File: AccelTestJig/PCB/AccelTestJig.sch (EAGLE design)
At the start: 11 parts, among them Q1 MMBTA56-SOT23, U1 MMA8653FCR1

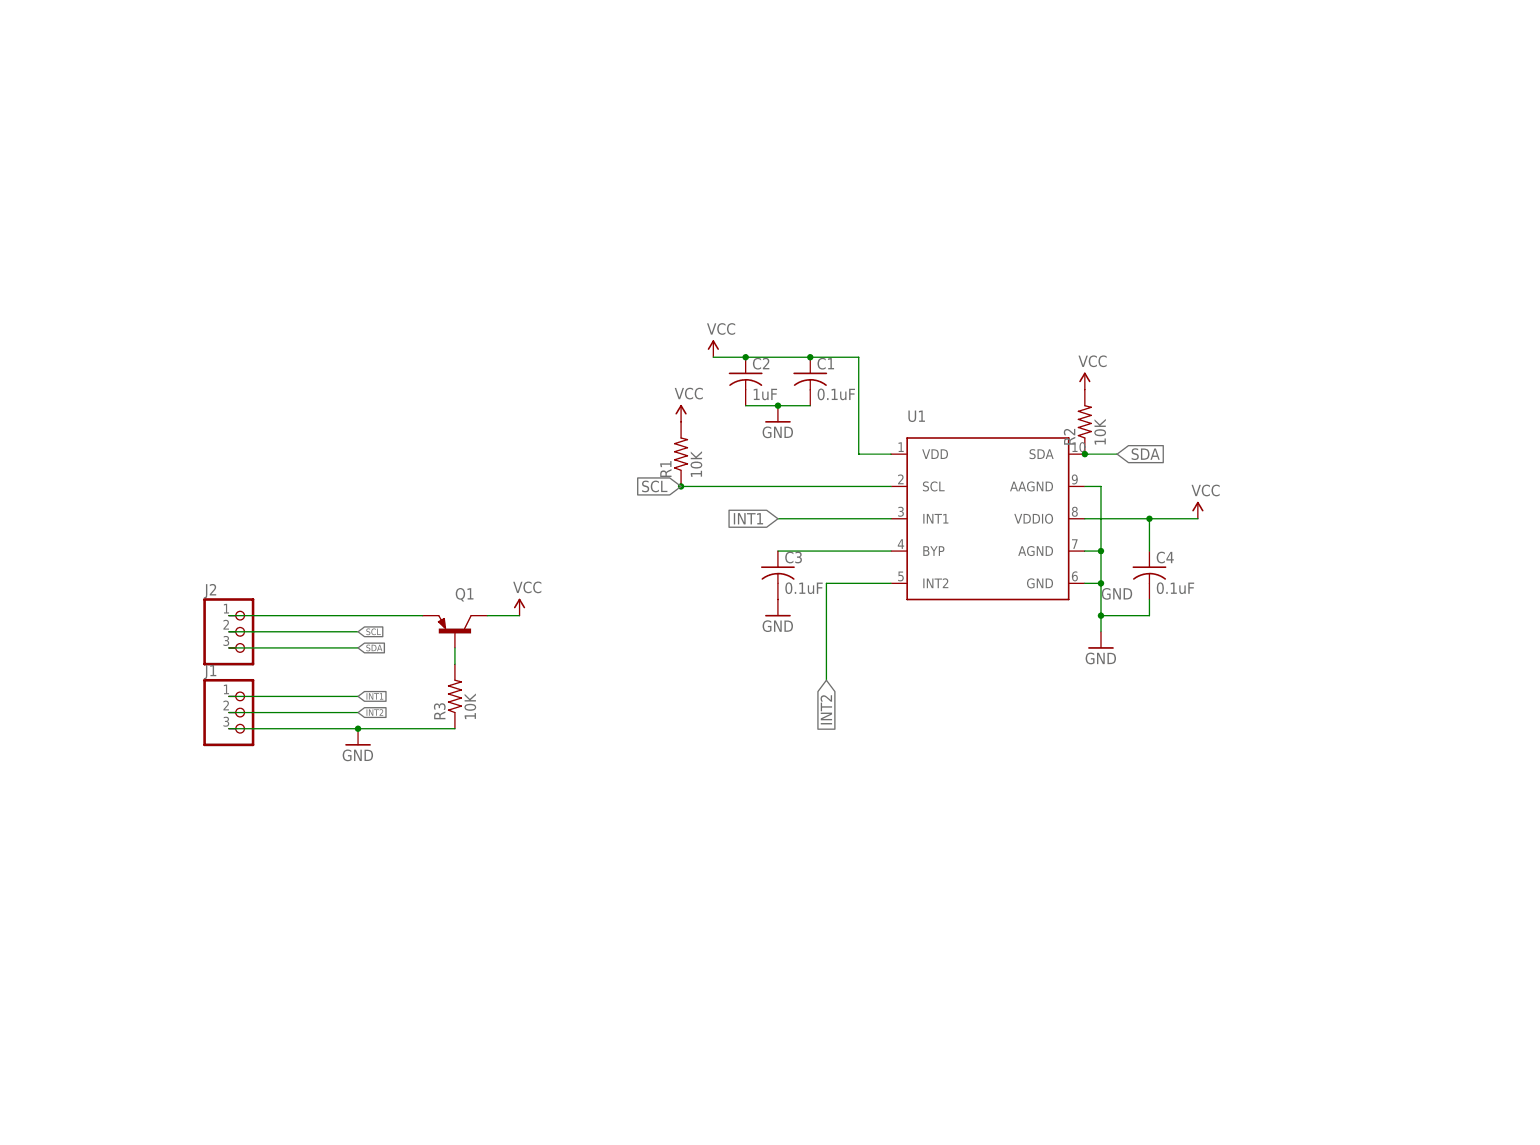
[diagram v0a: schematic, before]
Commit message: AccelTestJig - first rev (sent to oshpark)
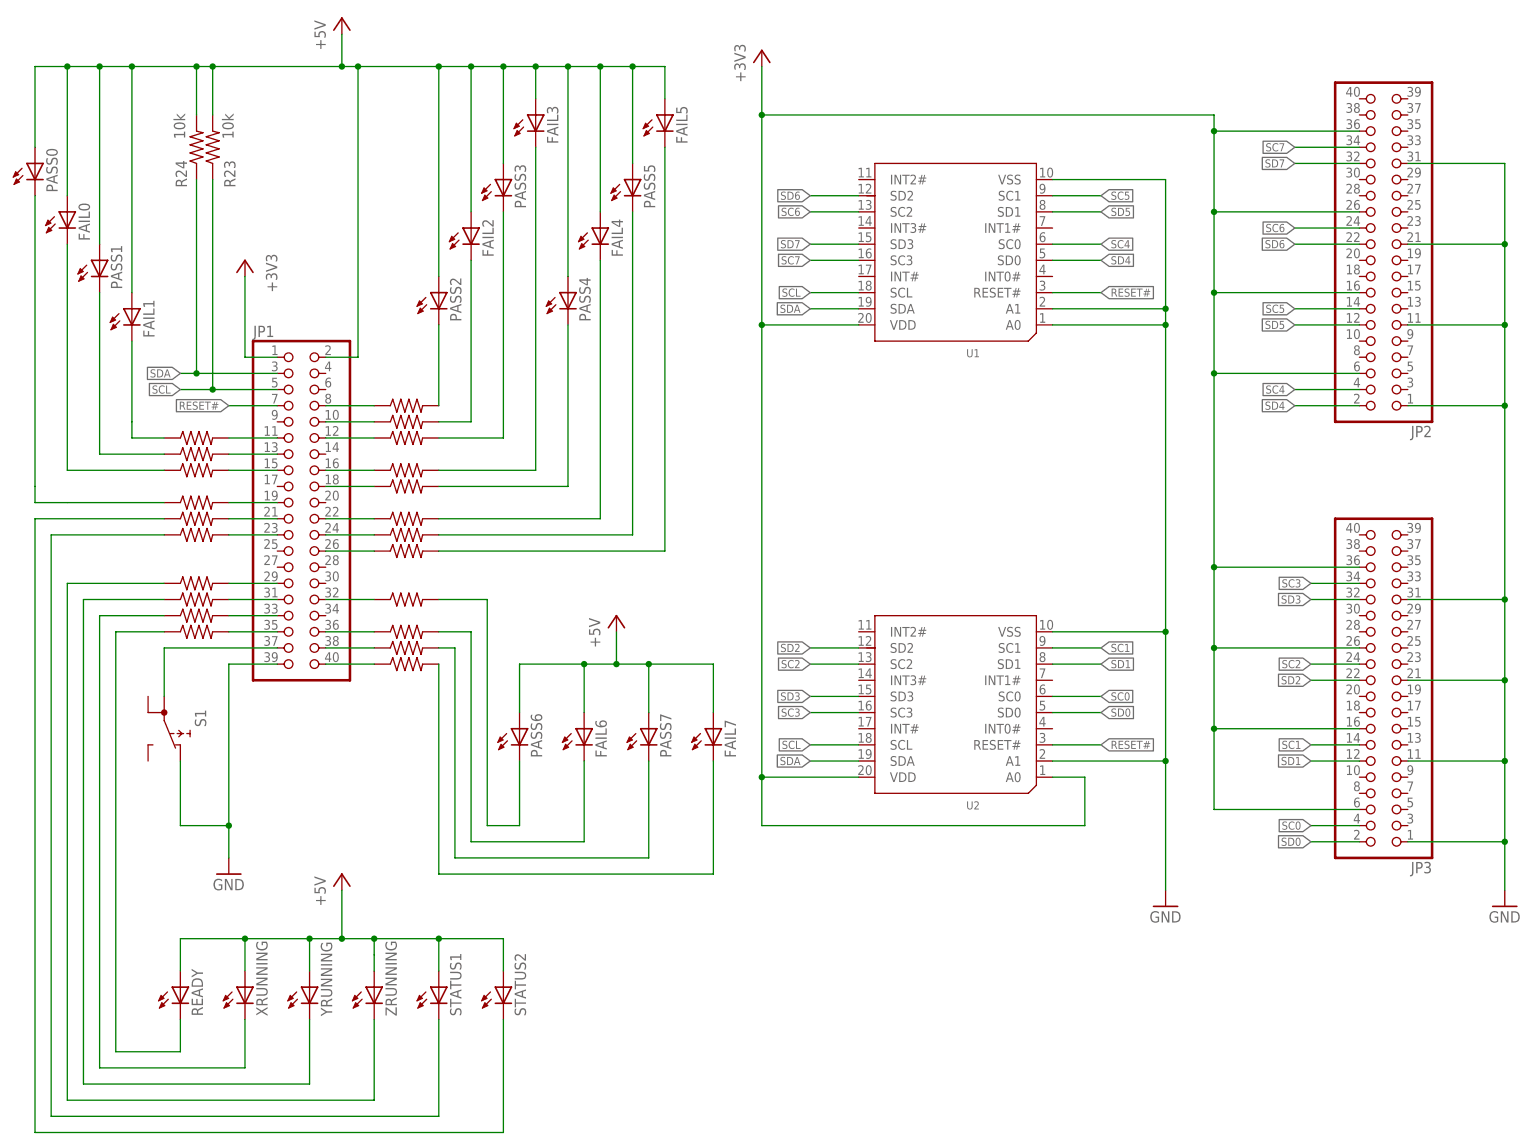
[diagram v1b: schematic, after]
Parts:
- removed C1, C3, C4: 0.1uF, AccelBreakout:C-USC0603
- removed C2: 1uF, AccelBreakout:C-USC0603
- removed J1, J2: (no value), AccelBreakout:PINHD-1X3
- removed Q1: MMBTA56-SOT23, transistor-pnp:MMBTA56-SOT23
- added FAIL0, FAIL1, FAIL2, FAIL3, FAIL4, FAIL5, FAIL6, FAIL7: FAIL, led:LEDCHIPLED_0805
- added JP1: NONE, AccelTestJig:PINHD-2X20
- added JP2, JP3: NONE, AccelTestJig:PINHD(2X20-WIDE)
- added PASS0, PASS1, PASS2, PASS3, PASS4, PASS5, PASS6, PASS7: PASS, led:LEDCHIPLED_0805
- added R10, R11, R12, R13, R14, R15, R16, R17, R18, R19, R20, R21, R22, R4, R5, R6, R7, R8, R9: 100, resistor:R-US_R0805
- added R23, R24: 10k, resistor:R-US_R0805
- added READY: READY, led:LEDCHIPLED_0805
- added S1: START, AccelTestJig:PUSHBUTTON(6X6SMD)01
- added STATUS1, STATUS2: NONE, led:LEDCHIPLED_0805
- added U2: NONE, AccelTestJig:PCA9545(SOIC20)
- added XRUNNING: TESTING X, led:LEDCHIPLED_0805
- added YRUNNING: TESTING Y, led:LEDCHIPLED_0805
- added ZRUNNING: TESTING Z, led:LEDCHIPLED_0805
- R1, R2, R3: value 10K -> 100; device AccelBreakout:R-US_R0603 -> resistor:R-US_R0805
- U1: value MMA8653FCR1 -> NONE; device AccelBreakout:MMA8653FCR1 -> AccelTestJig:PCA9545(SOIC20)
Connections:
- removed net INT1: J1.1, U1.INT1
- removed net INT2: J1.2, U1.INT2
- removed net VCC: C1.1, C2.1, C4.1, Q1.C, R1.2, R2.2, U1.VDD, U1.VDDIO
- new net +3V3: JP1.1, JP2.16, JP2.26, JP2.36, JP2.6, JP3.16, JP3.26, JP3.36, JP3.6, U1.VDD, U2.A0, U2.VDD
- new net +5V: FAIL0.A, FAIL1.A, FAIL2.A, FAIL3.A, FAIL4.A, FAIL5.A, FAIL6.A, FAIL7.A, JP1.2, PASS0.A, PASS1.A, PASS2.A, PASS3.A, PASS4.A, PASS5.A, PASS6.A, PASS7.A, R23.2, R24.2, READY.A, STATUS1.A, STATUS2.A, XRUNNING.A, YRUNNING.A, ZRUNNING.A
- new net N$13: FAIL7.C, R15.2
- new net N$14: FAIL1.C, R16.1
- new net N$15: PASS1.C, R17.1
- new net N$16: FAIL0.C, R18.1
- new net N$17: JP1.19, R19.2
- new net N$18: PASS0.C, R19.1
- new net N$19: JP1.8, R1.1
- new net N$20: JP1.10, R2.1
- new net N$21: JP1.12, R14.1
- new net N$22: PASS2.C, R1.2
- new net N$23: FAIL2.C, R2.2
- new net N$24: PASS3.C, R14.2
- new net N$25: FAIL3.C, R3.2
- new net N$26: PASS4.C, R4.2
- new net N$27: FAIL4.C, R5.2
- new net N$28: PASS5.C, R6.2
- new net N$29: FAIL5.C, R7.2
- new net N$3: JP1.15, R18.2
- new net N$30: PASS7.C, R10.2
- new net N$31: FAIL6.C, R9.2
- new net N$32: PASS6.C, R8.2
- new net N$33: JP1.16, R3.1
- new net N$35: JP1.22, R5.1
- new net N$36: JP1.24, R6.1
- new net N$37: JP1.26, R7.1
- new net N$38: JP1.32, R8.1
- new net N$39: JP1.36, R9.1
- new net N$40: JP1.38, R10.1
- new net N$41: JP1.40, R15.1
- new net N$42: R22.1, READY.C
- new net N$43: R21.1, XRUNNING.C
- new net N$44: R13.1, YRUNNING.C
- new net N$46: R11.1, STATUS1.C
- new net N$47: R20.1, STATUS2.C
- new net N$48: JP1.21, R20.2
- new net N$49: JP1.23, R11.2
- new net N$50: JP1.29, R12.2
- new net N$51: JP1.31, R13.2
- new net N$52: JP1.33, R21.2
- new net N$53: JP1.35, R22.2
- new net N$54: JP1.37, S1.1
- new net RESET#: JP1.7, U1.RESET#, U2.RESET#
- new net SC0: JP3.4, U2.SC0
- new net SC1: JP3.14, U2.SC1
- new net SC2: JP3.24, U2.SC2
- new net SC3: JP3.34, U2.SC3
- new net SC4: JP2.4, U1.SC0
- new net SC5: JP2.14, U1.SC1
- new net SC6: JP2.24, U1.SC2
- new net SC7: JP2.34, U1.SC3
- new net SD0: JP3.2, U2.SD0
- new net SD1: JP3.12, U2.SD1
- new net SD2: JP3.22, U2.SD2
- new net SD3: JP3.32, U2.SD3
- new net SD4: JP2.2, U1.SD0
- new net SD5: JP2.12, U1.SD1
- new net SD6: JP2.22, U1.SD2
- new net SD7: JP2.32, U1.SD3
- new net ZRUNNING: R12.1, ZRUNNING.C
- net GND: now also JP1.39, JP2.1, JP2.11, JP2.21, JP2.31, JP3.1, JP3.11, JP3.21, JP3.31, S1.2, U1.A0, U1.A1, U1.VSS, U2.A1, U2.VSS; no longer C1.2, C2.2, C3.2, C4.2, J1.3, R3.1, U1.AAGND, U1.AGND, U1.GND
- net N$1: now also JP1.11, R16.2; no longer J2.1, Q1.E
- net N$2: now also JP1.13, R17.2; no longer Q1.B, R3.2
- net N$34: now also JP1.18, R4.1; no longer C3.1, U1.BYP
- net SCL: now also JP1.5, R23.1, U2.SCL; no longer J2.2, R1.1
- net SDA: now also JP1.3, R24.1, U2.SDA; no longer J2.3, R2.1
